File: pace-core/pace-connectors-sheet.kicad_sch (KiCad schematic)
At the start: 31 parts, among them CN1 XT60PW-M, J2 Wiz5500-Coprocessor-BoB, Q1 BSS138, Q2 BSS138, Q3 BSS138, SW3 DPDT, U12 SM06B-SRSS-TB, U13 SM06B-SRSS-TB, U3 USBLC6-2P6, U4 ADUM3160BRWZ-RL

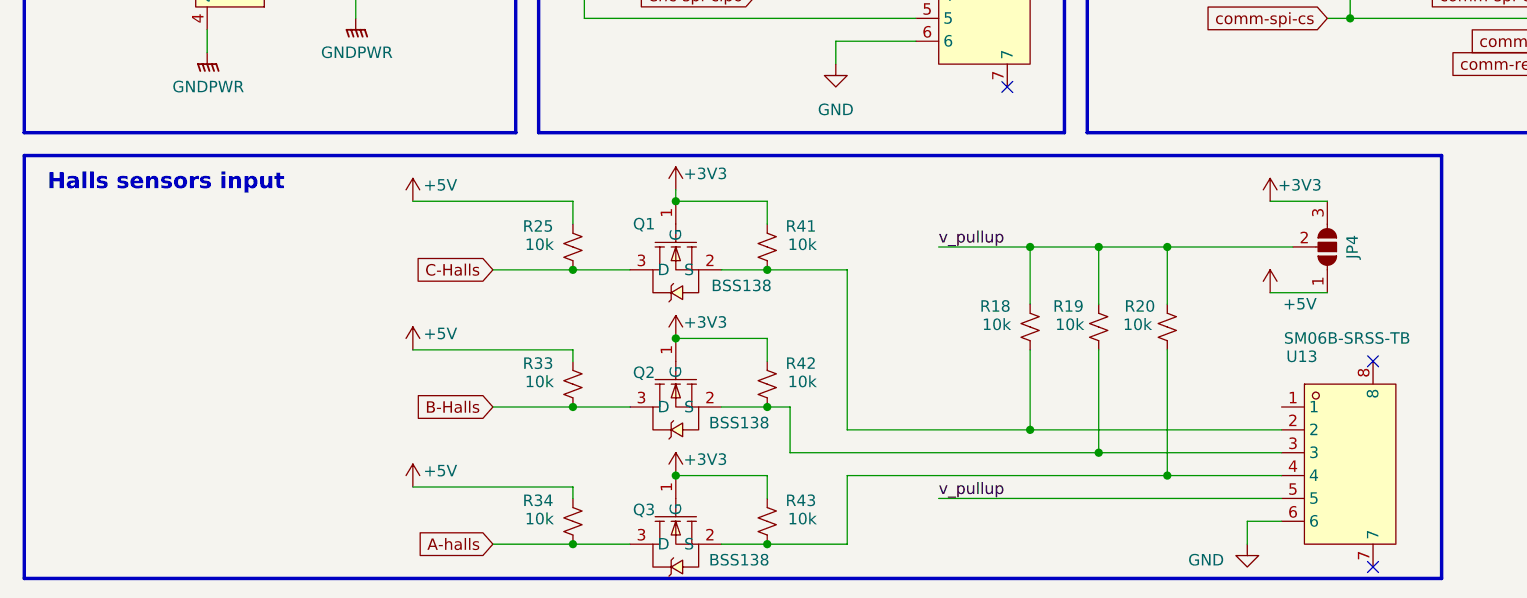
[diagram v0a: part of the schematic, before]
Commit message: update connectors schematic and PCB layout, refresh r2 STEP export
Co-Authored-By: Claude Fable 5 <noreply@anthropic.com>
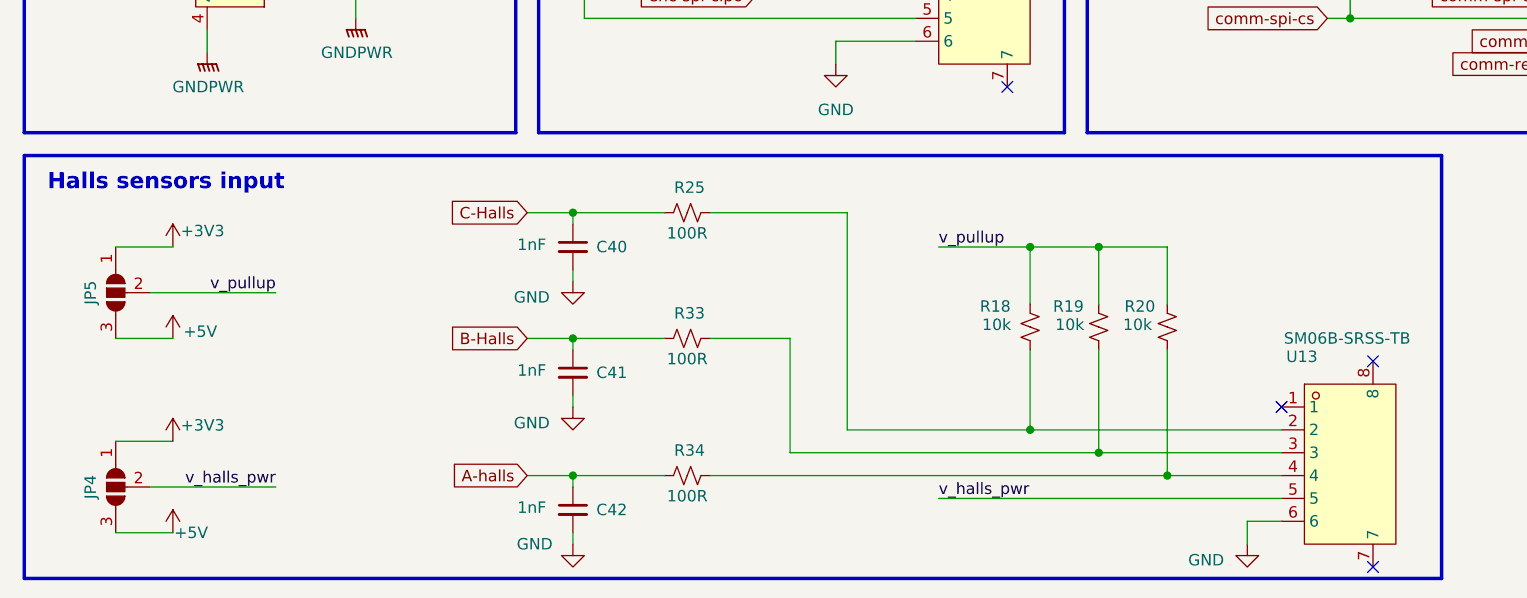
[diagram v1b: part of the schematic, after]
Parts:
- removed Q1, Q2, Q3: BSS138, specific-parts-lib:SOT-23-3_L2.9-W1.6-P1.90-LS2.8-BR, symbol specific-parts-lib:BSS138_C52895
- removed R41, R42, R43: 10k, Resistor_SMD:R_0402_1005Metric, symbol Device:R_Small_US
- added C40, C41, C42: 1nF, Capacitor_SMD:C_0402_1005Metric, symbol Device:C_Small
- added JP5: SolderJumper_3_Bridged12, Jumper:SolderJumper-3_P1.3mm_Open_RoundedPad1.0x1.5mm, symbol Jumper:SolderJumper_3_Open
- R25, R33, R34: value 10k -> 100R
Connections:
- net +3V3: now also JP4.1 (A), JP5.1 (A); no longer JP4.3 (B)
- net +5V: now also JP4.3 (B), JP5.3 (B); no longer JP4.1 (A), R25.2, R33.2, R34.2
- net A-halls: now also C42.1
- net B-Halls: now also C41.1
- net C-Halls: now also C40.1
- net GND: now also C40.2, C41.2, C42.2
- net v_pullup: now also JP5.2 (C); no longer JP4.2 (C), U13.5
- net at R20.1, U13.4: now also R34.2
- net at R18.1, U13.2: now also R25.2
- net at R19.1, U13.3: now also R33.2
- new net v_halls_pwr: JP4.2 (C), U13.5
- no-connect marks 9 -> 10

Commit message: Repo hygiene, CI as source of truth, and V1R2 design cleanup
Repository
- Sources only in pace-core/: untrack .history, lock files, .DS_Store,
  backups, layer PDFs, STEP exports, ibom. Regenerable outputs are
  gitignored; CI rebuilds them.
- Git LFS for Blender, PSD, video and curated renders (.gitattributes).
- Move brand artwork to graphics/, curated renders to docs/media/.
- Track the V1R2 fab package CSVs that the old gitignore hid.

CI
- KiBot builds gerbers, drill, fab zip, BOM (CSV/HTML with MPN and LCSC),
  position, ibom, IPC netlist, schematic and layer PDFs, DRC report,
  STEP and renders. REV is set from `git describe` on V*R* tags.
- ERC and DRC block PRs; tag builds publish a GitHub Release.
- README pin map is generated from the netlist (tools/gen_readme.py)
  and checked in CI.
- PR template with review checklist.

Design (ERC 0 errors, DRC 0 errors with schematic parity, netlist
connectivity verified identical across all 101 nets)
- Rename 49 nets to lowercase domain-kebab via tools/rename_nets.py.
- Add TITLE/PROJECT_CODE/REV/COMPANY text variables and title blocks on
  every sheet and the board.
- Net classes now carry both widths and colours: GND, 3V3, 5V, GND-USB,
  Batt, Motor-A/B/C. Remove High-Current-GND (its net never existed).
- Remove all 10 stale DRC exclusions; fold the shunt net-tie bridge copper
  into pad 2 and waive clearance around NT1..NT3 via pace-core.kicad_dru.
- Add Manufacturer/MPN/LCSC fields to every symbol and footprint.
- Fix capacitor symbols with input-typed pins, add PWR_FLAGs on GND and
  +BATT, convert duplicate local labels to global, complete the
  half-bridge bus alias, re-home symbols from missing libraries.

Docs
- docs/style-guide.md, decision records 0001-0003, errata, bring-up
  checklist. CLAUDE.md updated for the new layout and conventions.

Co-Authored-By: Claude Fable 5.1 <noreply@anthropic.com>
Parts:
- R4, R5, R6, R7: symbol sparkfun_resistors:RESISTOR0603 -> specific-parts-lib:RESISTOR0603
- U3: MPN (none) -> USBLC6-2P6; Manufacturer (none) -> STMicroelectronics
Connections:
- net A-halls renamed hall-a
- net B-Halls renamed hall-b
- net C-Halls renamed hall-c
- net comm-irq renamed eth-irq
- net comm-reset renamed eth-reset
- net comm-spi-cipo renamed spi-cipo
- net comm-spi-clk renamed spi-clk
- net comm-spi-copi renamed spi-copi
- net comm-spi-cs renamed eth-spi-cs
- net usb_d+ renamed usb-dp
- net usb_d- renamed usb-dm
- net v_halls_pwr renamed hall-vcc
- net v_pullup renamed hall-vpull
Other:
- company: (none) -> ${COMPANY}
- title: (none) -> ${TITLE} - Connectors
